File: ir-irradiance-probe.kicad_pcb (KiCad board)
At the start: 2 copper layers, 80 x 80 mm, 25 parts, among them J1 USB-C_USB4105-GF-A, J2 SM04B-SRSS-TB-LF-SN, J3 PinHeader_1x2_P2.54mm_Drill1.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, J4 PinHeader_1x3_P2.54mm_Drill1.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, J6 Conn_BNC_031-70526-21, U1 TLV70033_SC70, U2 LM339_TSSOP, U3 AP62301WU-7

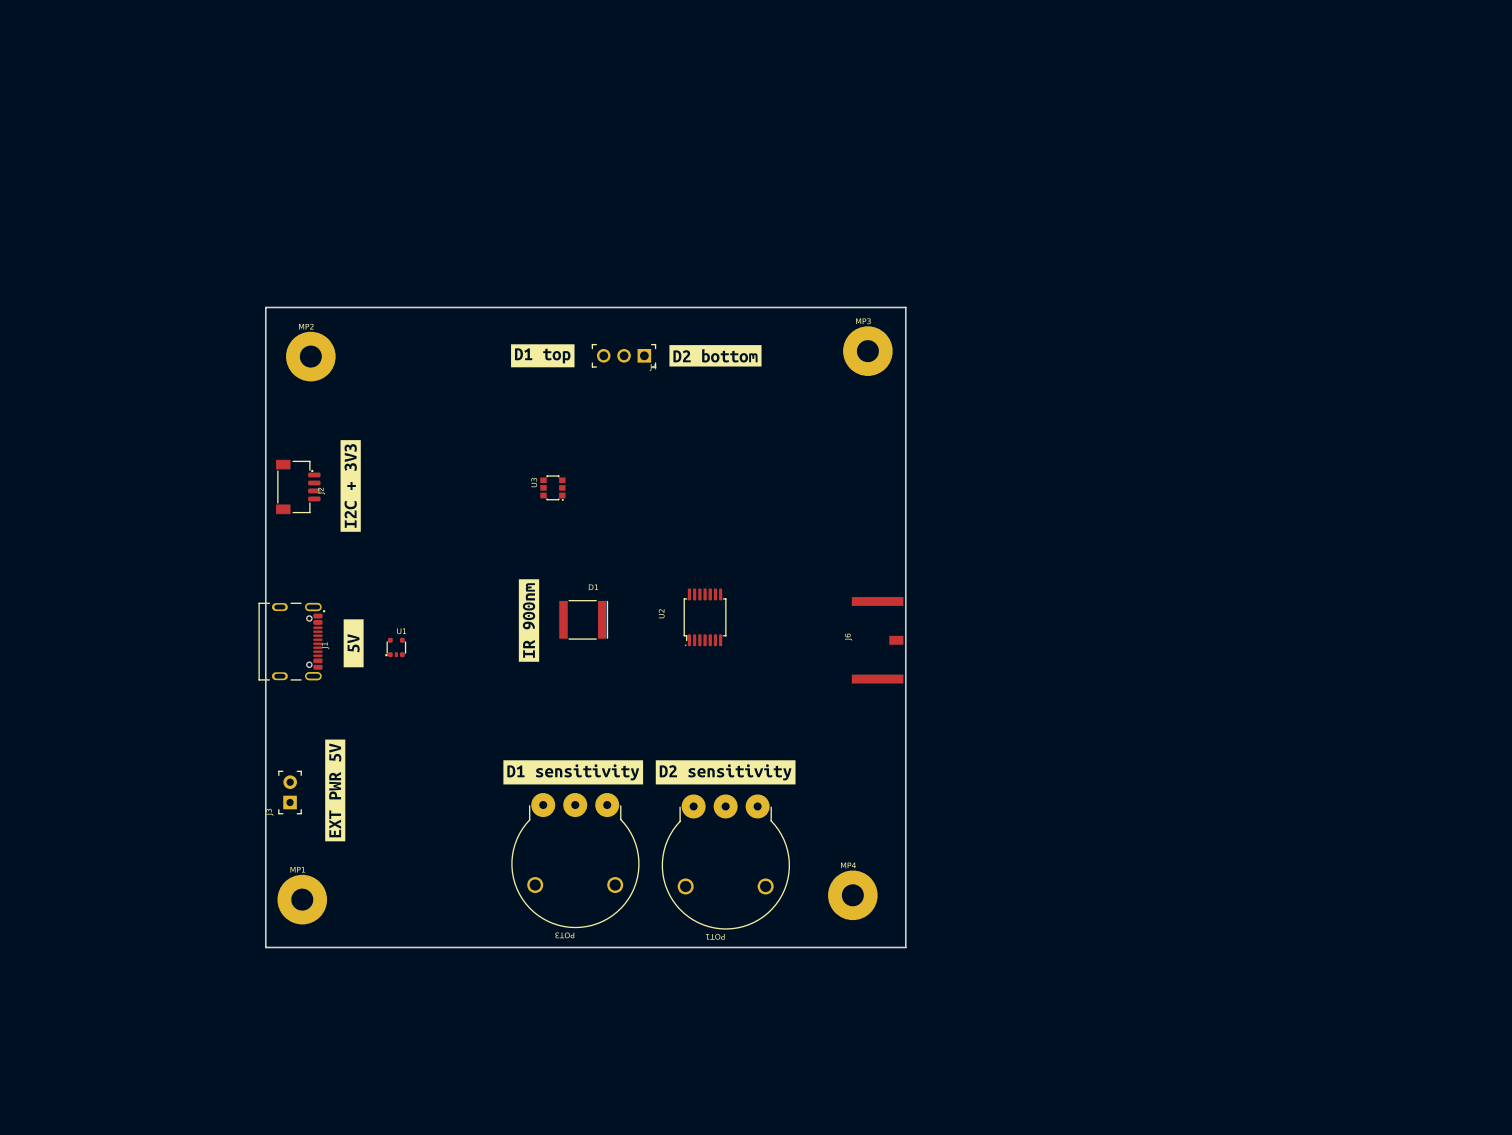
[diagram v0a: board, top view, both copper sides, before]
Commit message: [#47284] Migrated project back to KiCad v6
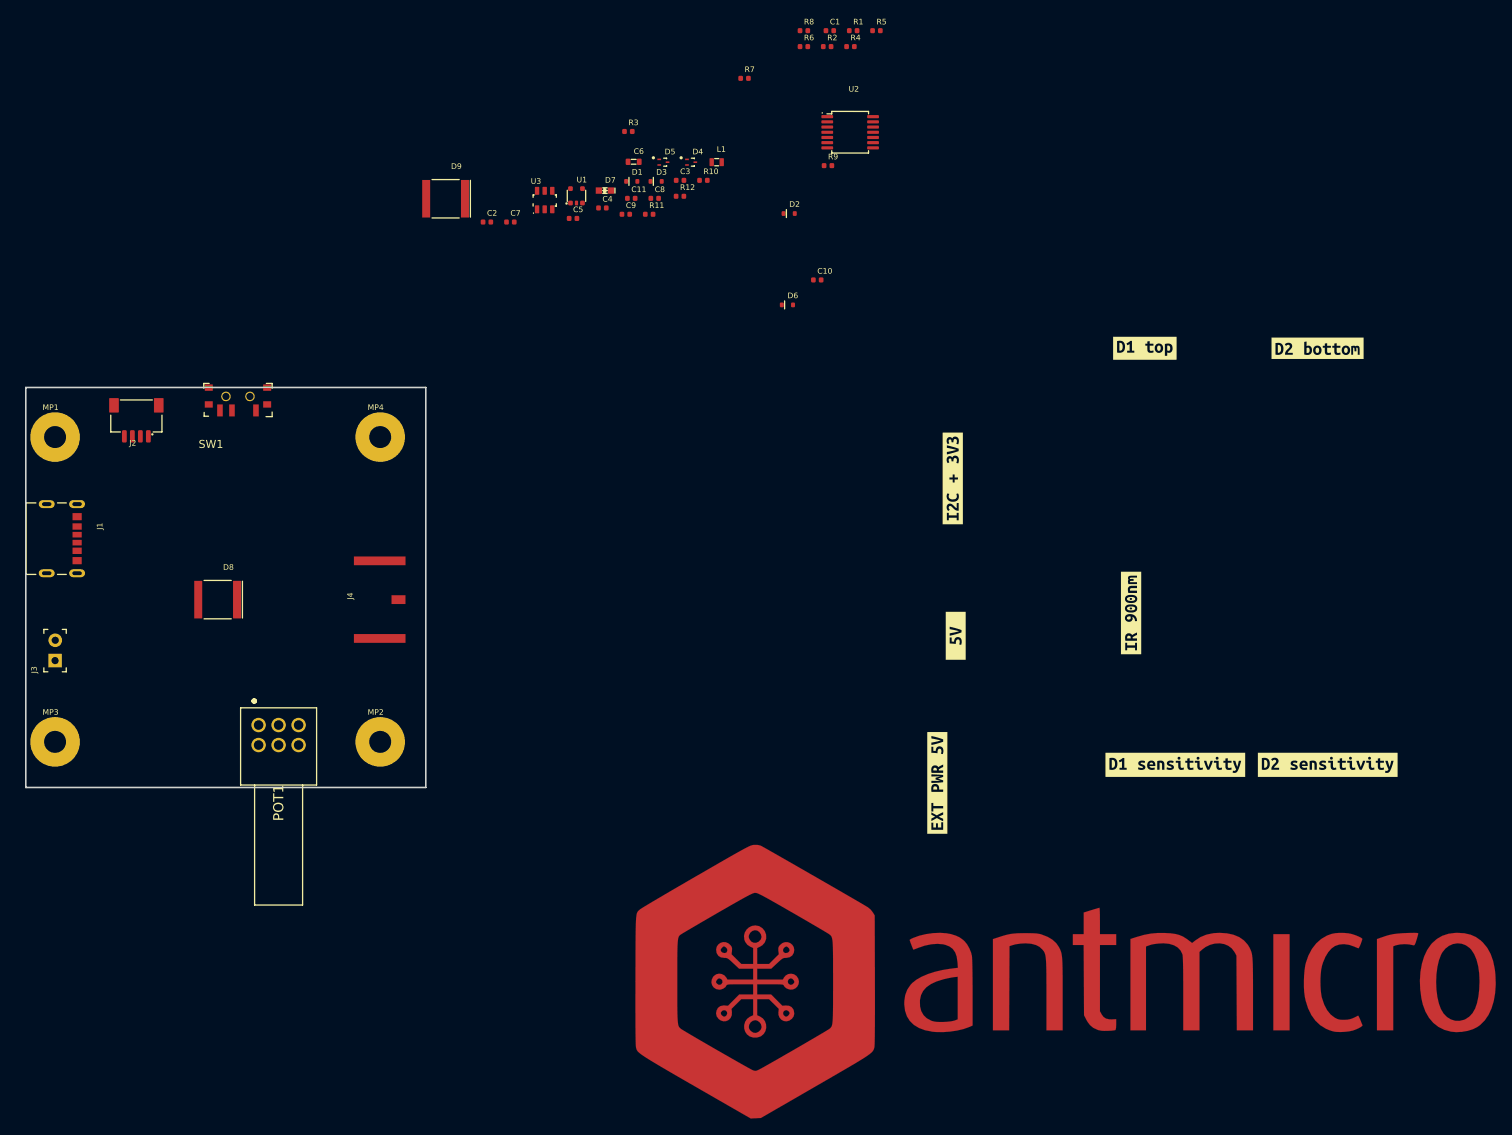
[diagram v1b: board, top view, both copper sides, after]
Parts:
- removed J6: Conn_BNC_031-70526-21, antmicro-footprints:Conn_BNC_031-70526-21
- removed POT3: POT_20k_R0141-2-20k, antmicro-footprints:POT_R0141-2
- added C1: C_1u_0402, antmicro-footprints:C_0402_1005Metric, F.Cu at (170.5, 25.4)
- added C10: C_180p_0402, antmicro-footprints:C_0402_1005Metric, F.Cu at (168.9, 56.6)
- added C11: C_180p_0402, antmicro-footprints:C_0402_1005Metric, F.Cu at (145.7, 46.4)
- added C2: C_1u_0402, antmicro-footprints:C_0402_1005Metric, F.Cu at (127.6, 49.3)
- added C3: C_1u_0402, antmicro-footprints:C_0402_1005Metric, F.Cu at (151.8, 44.1)
- added C4: C_1u_0402, antmicro-footprints:C_0402_1005Metric, F.Cu at (142.1, 47.6)
- added C5: C_100n_0402, antmicro-footprints:C_0402_1005Metric, F.Cu at (138.4, 48.9)
- added C6: C_4u7_0603, antmicro-footprints:C_0603_1608Metric, F.Cu at (146.0, 41.8)
- added C7: C_100n_0402, antmicro-footprints:C_0402_1005Metric, F.Cu at (130.6, 49.3)
- added C8: C_470p_0402, antmicro-footprints:C_0402_1005Metric, F.Cu at (148.6, 46.4)
- added C9: C_1n5_0402, antmicro-footprints:C_0402_1005Metric, F.Cu at (145.0, 48.4)
- added D3: RB521S30T1G, antmicro-footprints:SOD-523, F.Cu at (148.8, 44.2)
- added D4: PESD5V0S2BQA, antmicro-footprints:TPD2E009DRTR, F.Cu at (153.2, 41.8)
- added D5: PESD5V0S2BQA, antmicro-footprints:TPD2E009DRTR, F.Cu at (149.7, 41.8)
- added D6: RB521S30T1G, antmicro-footprints:SOD-523, F.Cu at (165.2, 59.7)
- added D7: LED_G_0603_LTST-C190GKT, antmicro-footprints:LED_0603_1608Metric_G, F.Cu at (142.4, 45.4)
- added D8: TEMD5020X01, antmicro-footprints:Photodiode_SMD_4.2x5mm_TEMD, F.Cu at (94.0, 96.5)
- added D9: TEMD5020X01, antmicro-footprints:Photodiode_SMD_4.2x5mm_TEMD, F.Cu at (122.5, 46.4)
- added L1: L_2u2_0.2A_0603, antmicro-footprints:L_0603_1608Metric, F.Cu at (156.4, 41.8)
- added N1: antmicro_logo, antmicro-footprints:antmicro-logo, F.Cu at (203.2, 144.8)
- added R1: R_5k1_0402, antmicro-footprints:R_0402_1005Metric, F.Cu at (173.4, 25.4)
- added R10: R_47k_0402, antmicro-footprints:R_0402_1005Metric, F.Cu at (154.7, 44.1)
- added R11: R_10k_0402, antmicro-footprints:R_0402_1005Metric, F.Cu at (147.9, 48.4)
- added R12: R_47k_0402, antmicro-footprints:R_0402_1005Metric, F.Cu at (151.8, 46.1)
- added R2: R_5k1_0402, antmicro-footprints:R_0402_1005Metric, F.Cu at (170.2, 27.4)
- added R3: R_1k2_0402, antmicro-footprints:R_0402_1005Metric, F.Cu at (145.3, 38.0)
- added R4: R_22R_0402, antmicro-footprints:R_0402_1005Metric, F.Cu at (173.1, 27.4)
- added R5: R_0R_0402, antmicro-footprints:R_0402_1005Metric, F.Cu at (176.3, 25.4)
- added R6: R_5k1_0402, antmicro-footprints:R_0402_1005Metric, F.Cu at (167.3, 27.4)
- added R7: R_5k1_0402, antmicro-footprints:R_0402_1005Metric, F.Cu at (159.8, 31.4)
- added R8: R_1k_0402, antmicro-footprints:R_0402_1005Metric, F.Cu at (167.3, 25.4)
- added R9: R_10k_0402, antmicro-footprints:R_0402_1005Metric, F.Cu at (170.3, 42.3)
- added SW1: MSS3-V-T_R, antmicro-footprints:Switch_Slide_MSS3, F.Cu at (96.5, 71.1)
- D1: value TEMD5020X01 -> RB521S30T1G; footprint antmicro-footprints:Photodiode_SMD_4.2x5mm_TEMD -> antmicro-footprints:SOD-523
- D2: value TEMD5110X01 -> RB521S30T1G; footprint antmicro-footprints:Photodiode_SMD_4.2x5mm_TEMD -> antmicro-footprints:SOD-523; moved to F.Cu
- J1: value USB-C_USB4105-GF-A -> USB-C_UJC-HP-3-SMT-TR; footprint antmicro-footprints:USB-C_GCT_USB4105-GF-A -> antmicro-footprints:USB-C_UJC-HP-3-SMT-TR
- J4: value PinHeader_1x3_P2.54mm_Drill1.1mm -> Conn_BNC_031-70526-21; footprint antmicro-footprints:PinHeader_1x3_P2.54_Drill1.1mm -> antmicro-footprints:Conn_BNC_031-70526-21
- POT1: value POT_20k_R0141-2-20k -> PTD902-1015K-B104; footprint antmicro-footprints:POT_R0141-2 -> antmicro-footprints:PTD902-1015K-B104
- U2: value LM339_TSSOP -> AD8604ARUZ
- U3: value AP62301WU-7 -> ADC101C027CIMK; footprint antmicro-footprints:AP62301WU-7-TSOT23-6 -> antmicro-footprints:SOT-23-6
- moved MP3 112.7 mm to (73.7, 114.3)
- moved MP4 82.3 mm to (114.3, 76.2)
- moved kibuzzard-64C24EFD 75.3 mm to (232.7, 117.2)
- moved kibuzzard-64C24DFB 75.3 mm to (186.2, 101.0)
- moved kibuzzard-64C24E0E 75.3 mm to (185.9, 81.4)
- moved kibuzzard-64C24E25 75.3 mm to (183.9, 119.4)
- moved kibuzzard-64C24E37 75.3 mm to (208.2, 98.2)
- moved kibuzzard-64C24E46 75.3 mm to (208.1, 98.2)
- moved kibuzzard-64C24E71 75.3 mm to (209.9, 65.1)
- moved kibuzzard-64C24E83 75.3 mm to (231.5, 65.1)
- moved kibuzzard-64C24EE1 75.3 mm to (213.7, 117.2)
- moved MP1 65.6 mm to (73.7, 76.2)
- moved U2 63.3 mm to (173.0, 38.1), turned to 0 degrees
- moved POT1 63.2 mm to (99.1, 112.2), turned to -90 degrees
- moved U1 60.8 mm to (138.8, 46.0)
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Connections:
- D1 pad 1: unconnected-(D1-Pad1) -> Net-(C2-Pad2)
- D1 pad 2: unconnected-(D1-Pad2) -> /5V_USB
- D2 pad 1: unconnected-(D2-Pad1) -> Net-(C2-Pad2)
- D2 pad 2: unconnected-(D2-Pad2) -> /5V_PWR_SUPPLY
- J1 pad A12: Net-(J1-PadA1) -> GND
- J1 pad A5: unconnected-(J1-PadA5) -> Net-(J1-PadA5)
- J1 pad A9: Net-(J1-PadA4) -> /5V_USB
- J1 pad B12: Net-(J1-PadA1) -> GND
- J1 pad B5: unconnected-(J1-PadB5) -> Net-(J1-PadB5)
- J1 pad B9: Net-(J1-PadA4) -> /5V_USB
- J1 pad SH: unconnected-(J1-PadSH) -> GND
- J2 pad 1: unconnected-(J2-Pad1) -> GND
- J2 pad 2: unconnected-(J2-Pad2) -> /3V3_JST
- J2 pad 3: unconnected-(J2-Pad3) -> /SDA
- J2 pad 4: unconnected-(J2-Pad4) -> /SCL
- J2 pad S1: Net-(J2-PadS1) -> GND
- J2 pad S2: Net-(J2-PadS1) -> GND
- J3 pad 1: unconnected-(J3-Pad1) -> /5V_PWR_SUPPLY
- J3 pad 2: unconnected-(J3-Pad2) -> GND
- J4 pad 1: unconnected-(J4-Pad1) -> Net-(J4-Pad1)
- J4 pad 2: unconnected-(J4-Pad2) -> GND
- POT1 pad 1: unconnected-(POT1-Pad1) -> Net-(POT1-Pad1)
- POT1 pad 2: unconnected-(POT1-Pad2) -> /IR_900nm_OP_AMP_OUT
- POT1 pad 3: unconnected-(POT1-Pad3) -> /IR_900nm_OP_AMP_OUT
- U1 pad 1: unconnected-(U1-Pad1) -> /5V_FILTERED
- U1 pad 2: unconnected-(U1-Pad2) -> GND
- U1 pad 3: unconnected-(U1-Pad3) -> /5V_FILTERED
- U1 pad 5: unconnected-(U1-Pad5) -> Net-(C3-Pad2)
- U2 pad 1: unconnected-(U2-Pad1) -> /IR_900nm_OP_AMP_OUT
- U2 pad 10: unconnected-(U2-Pad10) -> GND
- U2 pad 11: unconnected-(U2-Pad11) -> GND
- U2 pad 12: unconnected-(U2-Pad12) -> /SELECTED_IR_SIG_FILTERED
- U2 pad 13: unconnected-(U2-Pad13) -> /ADC_IR_SIG_IN
- U2 pad 14: unconnected-(U2-Pad14) -> /ADC_IR_SIG_IN
- U2 pad 2: unconnected-(U2-Pad2) -> Net-(C10-Pad1)
- U2 pad 3: unconnected-(U2-Pad3) -> GND
- U2 pad 4: unconnected-(U2-Pad4) -> +3.3VA
- U2 pad 5: unconnected-(U2-Pad5) -> /SELECTED_IR_SIG
- U2 pad 6: unconnected-(U2-Pad6) -> Net-(J4-Pad1)
- U2 pad 7: unconnected-(U2-Pad7) -> Net-(J4-Pad1)
- U2 pad 8: unconnected-(U2-Pad8) -> /IR_900nm_OP_AMP_OUT
- U2 pad 9: unconnected-(U2-Pad9) -> Net-(C11-Pad1)
- U3 pad 1: unconnected-(U3-Pad1) -> +3.3VA
- U3 pad 2: unconnected-(U3-Pad2) -> GND
- U3 pad 3: unconnected-(U3-Pad3) -> Net-(C8-Pad1)
- U3 pad 4: unconnected-(U3-Pad4) -> Net-(R5-Pad2)
- U3 pad 5: unconnected-(U3-Pad5) -> /SCL
- U3 pad 6: unconnected-(U3-Pad6) -> /SDA
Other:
- board size 80 x 80 mm -> 50 x 50 mm

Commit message: [#47284] Prepare preliminary components layout
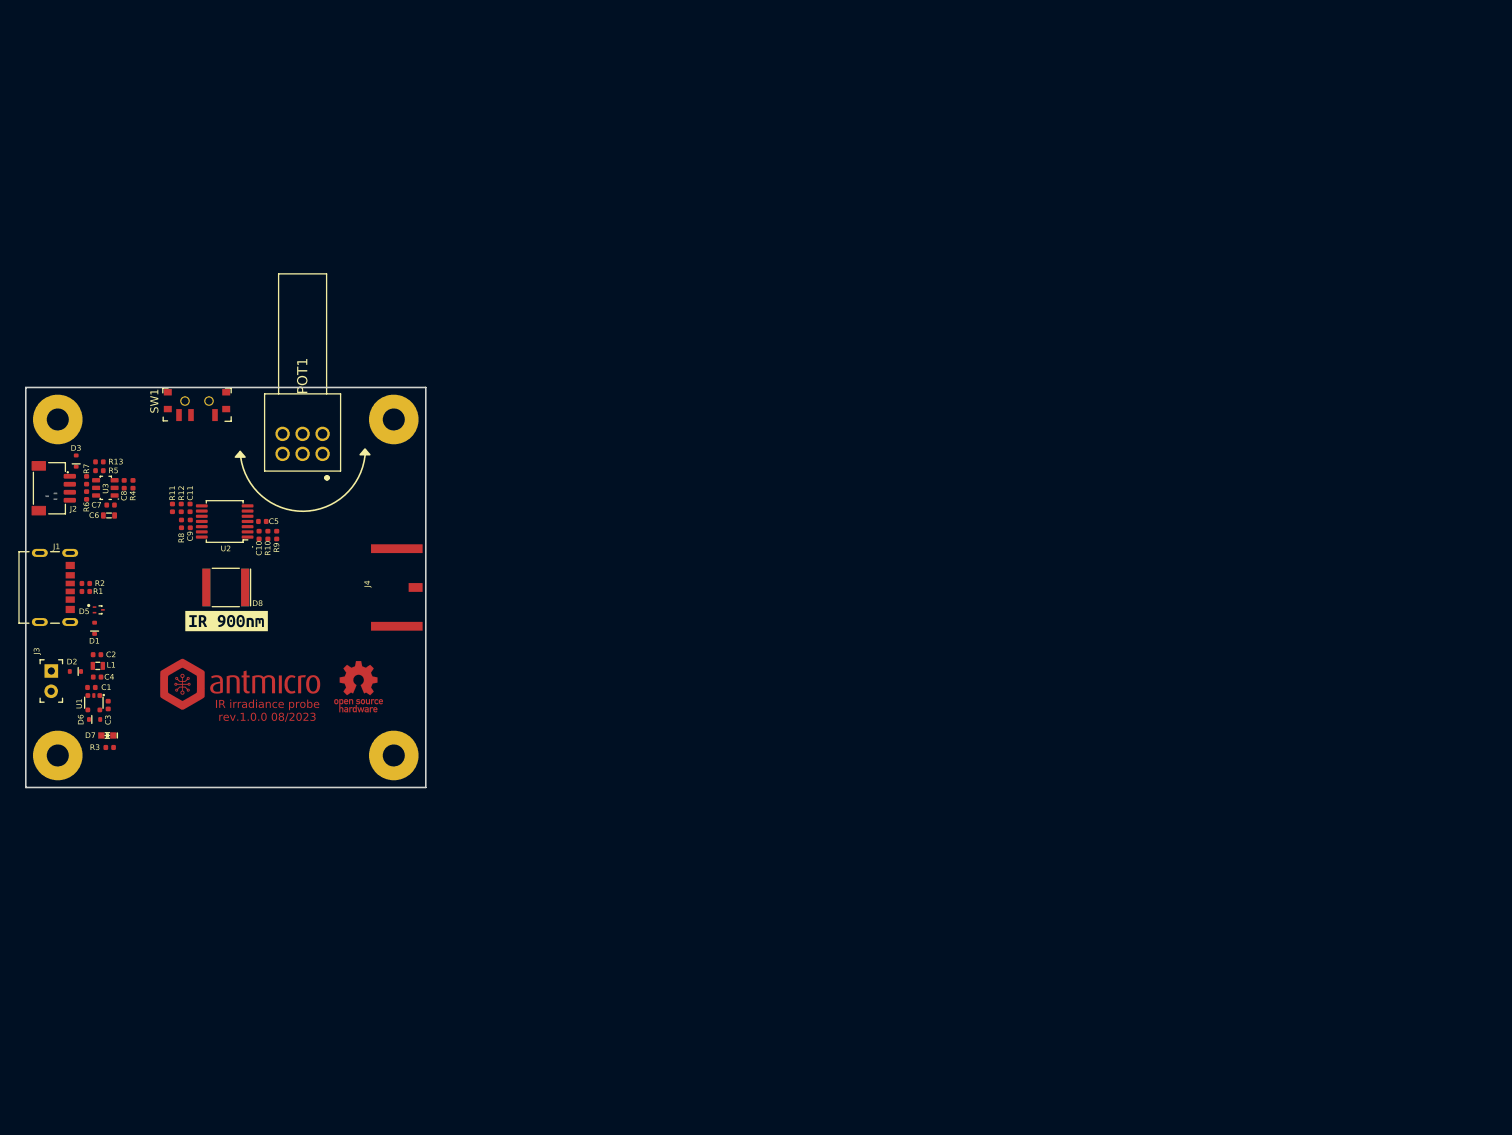
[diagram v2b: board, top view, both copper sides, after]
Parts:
- removed kibuzzard-64C24E71: G***, kibuzzard-64C24E71
- removed kibuzzard-64C24E83: G***, kibuzzard-64C24E83
- removed kibuzzard-64C24EE1: G***, kibuzzard-64C24EE1
- removed kibuzzard-64C24EFD: G***, kibuzzard-64C24EFD
- added N2: oshw_logo, antmicro-footprints:oshw-logo, F.Cu at (111.6, 107.4)
- added R13: R_0R_0402, antmicro-footprints:R_0402_1005Metric, F.Cu at (79.2, 79.3)
- D4, D9, kibuzzard-64C24DFB, kibuzzard-64C24E0E, kibuzzard-64C24E25: moved to B.Cu
- N1: footprint antmicro-footprints:antmicro-logo -> antmicro-footprints:antmicro-logo_scaled_20mm
- moved C1 123.5 mm to (78.2, 107.5), turned to 180 degrees
- moved R1 118.8 mm to (77.5, 95.5)
- moved R2 114.4 mm to (77.5, 94.5), turned to 180 degrees
- moved kibuzzard-64C24E37 113.1 mm to (95.1, 99.2), turned to 0 degrees
- moved kibuzzard-64C24E46 113.0 mm to (95.1, 99.2), turned to 180 degrees
- moved N1 112.8 mm to (96.8, 107.3)
- moved R5 111.6 mm to (79.2, 80.4), turned to 180 degrees
- moved kibuzzard-64C24E0E 109.1 mm to (76.8, 82.9)
- moved kibuzzard-64C24DFB 108.1 mm to (78.3, 94.9)
- moved kibuzzard-64C24E25 108.1 mm to (76.6, 106.6)
- moved D2 106.0 mm to (76.2, 105.5), turned to 180 degrees
- moved R6 105.8 mm to (77.6, 83.5), turned to -90 degrees
- moved R4 105.1 mm to (83.4, 82.1), turned to -90 degrees
- moved D6 100.9 mm to (78.6, 111.5)
- moved R3 100.7 mm to (80.5, 115.0)
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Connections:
- C11 pad 2: /IR_900nm_OP_AMP_OUT -> /IR_940nm_OP_AMP_OUT
- POT1 pad 5: /IR_900nm_OP_AMP_OUT -> /IR_940nm_OP_AMP_OUT
- POT1 pad 6: /IR_900nm_OP_AMP_OUT -> /IR_940nm_OP_AMP_OUT
- R12 pad 2: /IR_900nm_OP_AMP_OUT -> /IR_940nm_OP_AMP_OUT
- SW1 pad 3: /IR_900nm_OP_AMP_OUT -> /IR_940nm_OP_AMP_OUT
- U2 pad 8: /IR_900nm_OP_AMP_OUT -> /IR_940nm_OP_AMP_OUT
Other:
- board text added: "IR irradiance probe rev.1.0.0 08/2023"

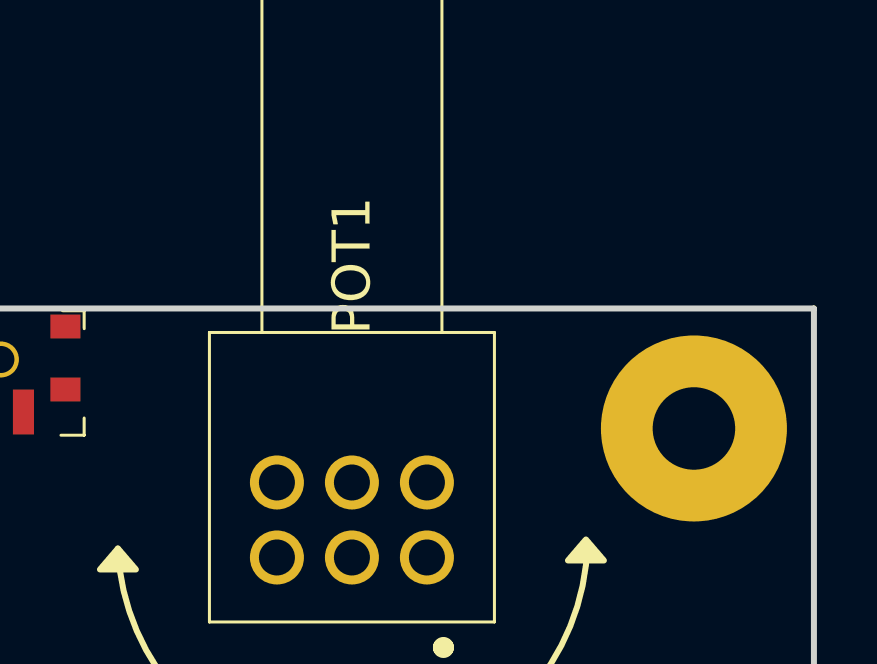
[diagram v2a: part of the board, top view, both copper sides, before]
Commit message: [#47284] Update potentiometer after standardisation
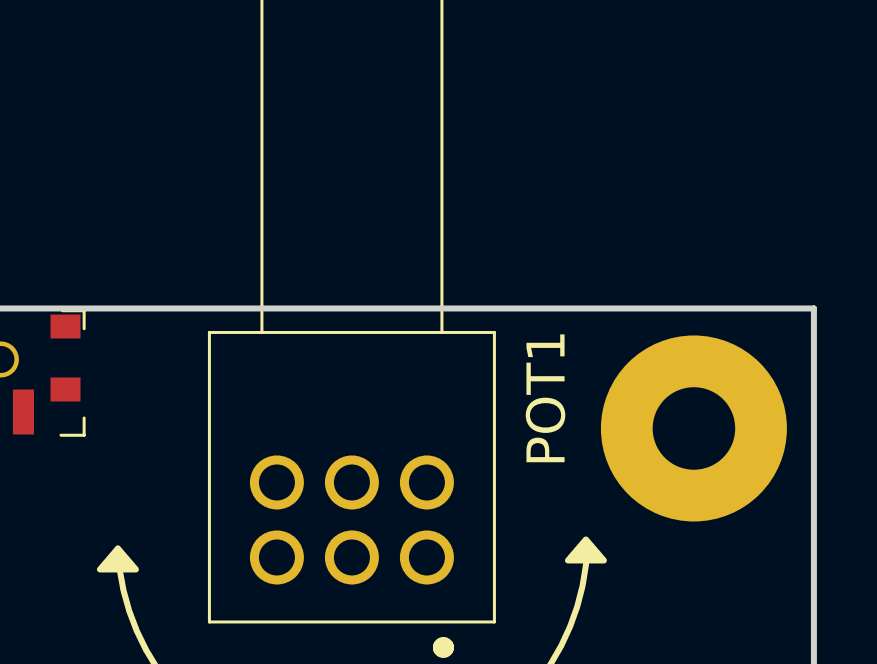
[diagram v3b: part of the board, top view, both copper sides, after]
